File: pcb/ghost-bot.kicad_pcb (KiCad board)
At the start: 2 copper layers, 111 x 60 mm, 35 parts, among them J1 Conn_01x03_Pin, J2 Conn_01x03_Pin, J3 Conn_01x04_Pin, J4 Conn_01x02_Pin, SW1 SW_Push, SW2 SW_Push, SW3 SW_SPDT

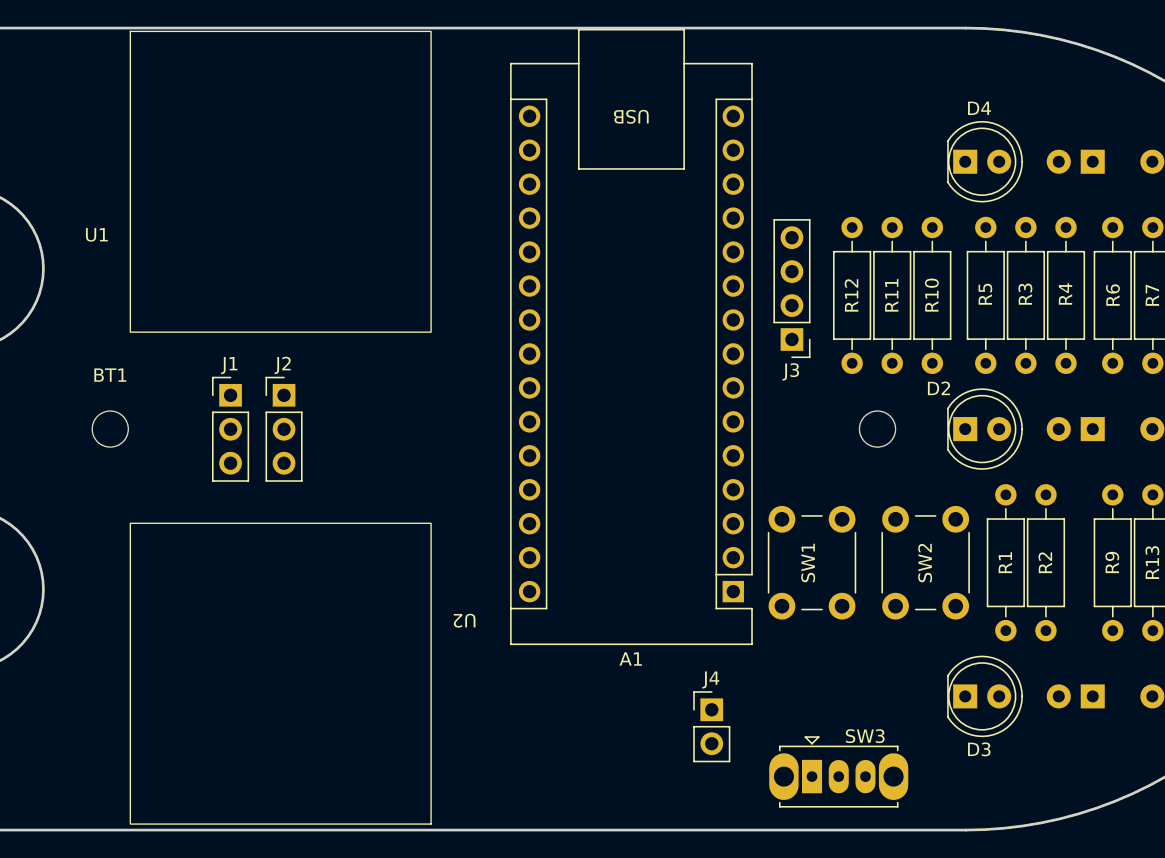
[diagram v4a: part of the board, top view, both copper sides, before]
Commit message: Minor placement changes, add strain relief for battery wires
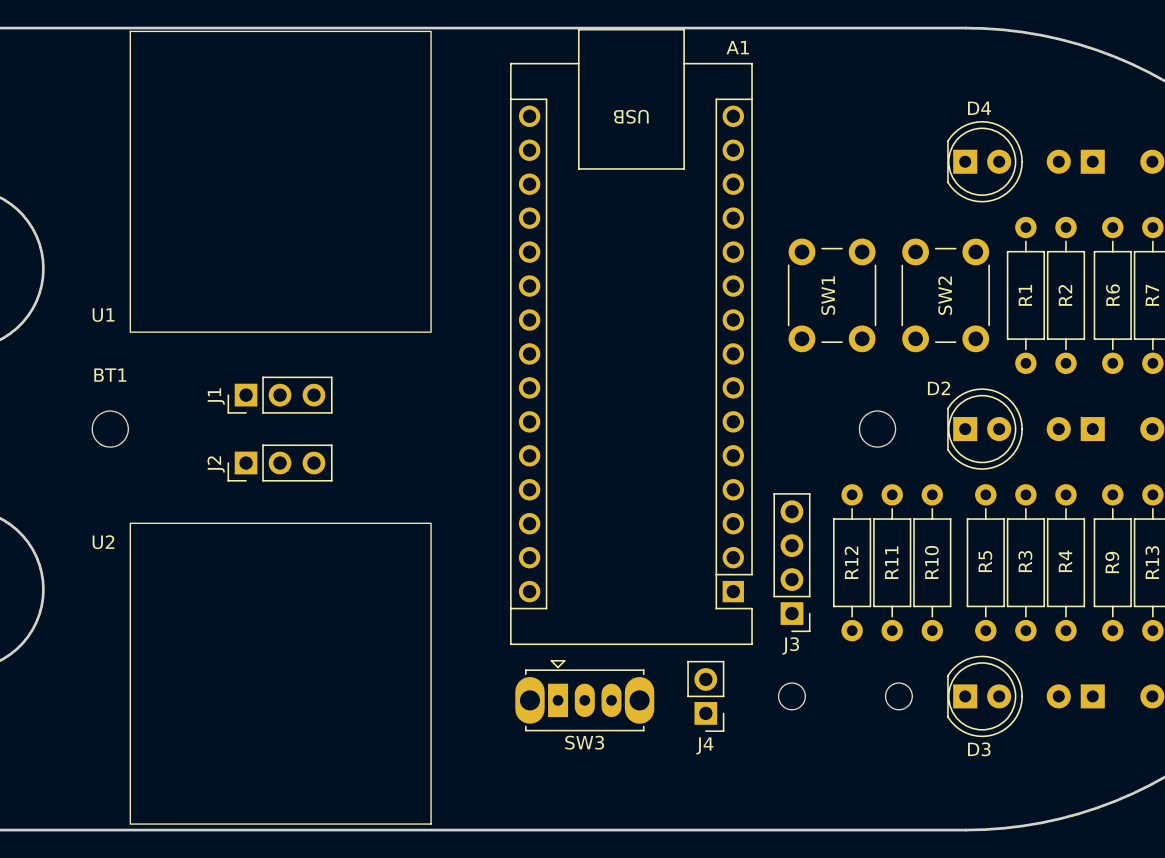
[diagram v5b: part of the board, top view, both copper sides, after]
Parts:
- added REF**: MountingHole_2.1mm, MountingHole:MountingHole_2.1mm, F.Cu at (169.5, 134.0)
- added REF**: MountingHole_2.1mm, MountingHole:MountingHole_2.1mm, F.Cu at (177.5, 134.0)
- moved J3 20.5 mm to (169.5, 127.8)
- moved R1 20.1 mm to (187.0, 109.1)
- moved R2 20.1 mm to (190.0, 109.1)
- moved SW1 20.1 mm to (170.3, 107.2)
- moved SW2 20.1 mm to (183.3, 100.8)
- moved R10 20.0 mm to (180.0, 129.1)
- moved R11 20.0 mm to (177.0, 129.1)
- moved R12 20.0 mm to (174.0, 129.1)
- moved R3 20.0 mm to (187.0, 129.1)
- moved R4 20.0 mm to (190.0, 129.1)
- moved R5 20.0 mm to (184.0, 129.1)
- moved SW3 19.8 mm to (152.0, 134.3)
- moved J2 5.81 mm to (128.7, 116.5), turned to 90 degrees
- moved J1 1.16 mm to (128.7, 111.5), turned to 90 degrees
- moved J4 0.52 mm to (163.1, 135.3), turned to 180 degrees

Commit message: WIP commit before changing layout
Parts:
- moved J1 5.08 mm to (128.7, 116.5)
- moved J2 5.08 mm to (128.7, 111.5)
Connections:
- A1 pad 21: /PD2 -> unconnected-(A1-A2-Pad21)
- A1 pad 26: unconnected-(A1-A7-Pad26) -> /PD2
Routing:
- net /PD2: track 0.00 -> 53.2 mm
- net /LED2: track 0.00 -> 52.5 mm
- net /PUSH_BTN1: track 0.00 -> 37.8 mm
- net /PUSH_BTN0: track 0.00 -> 30.7 mm
- net /LED0: track 0.00 -> 22.5 mm
- net /LED1: track 0.00 -> 20.6 mm

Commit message: Add initial routing
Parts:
- moved J3 44.5 mm to (128.7, 110.2), turned to 90 degrees
- moved REF** 27.5 mm to (150.0, 133.8), turned to 0 degrees
- moved R12 25.3 mm to (189.5, 109.1)
- moved R5 21.7 mm to (192.5, 109.1)
- moved R10 21.5 mm to (199.0, 118.9), turned to -90 degrees
- moved R9 21.2 mm to (186.5, 109.1)
- moved SW1 21.0 mm to (179.3, 126.2), turned to 180 degrees
- moved R4 15.7 mm to (202.0, 118.9), turned to -90 degrees
- moved R11 12.5 mm to (189.5, 129.1)
- moved R2 12.3 mm to (183.0, 98.9), turned to -90 degrees
- moved D2 12.3 mm to (194.7, 114.0)
- moved D3 12.3 mm to (194.7, 134.0)
- moved D4 12.3 mm to (194.7, 94.0)
- moved REF** 11.5 mm to (158.0, 133.8), turned to 0 degrees
- moved R14 10.7 mm to (196.0, 118.9), turned to -90 degrees
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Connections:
- A1 pad 12: /RGB_R -> /RGB_B
- A1 pad 14: /RGB_B -> /RGB_R
- A1 pad 20: /PD1 -> unconnected-(A1-A1-Pad20)
- A1 pad 25: unconnected-(A1-A6-Pad25) -> /PD1
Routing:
- net /PD1: track 0.00 -> 49.6 mm
- net /TRIG: track 0.00 -> 48.1 mm
- net /RGB_R: track 0.00 -> 45.8 mm
- net /RGB_G: track 0.00 -> 44.8 mm
- net /RGB_B: track 0.00 -> 43.6 mm
- net /PD0: track 0.00 -> 41.6 mm
- net /SERVO0: track 0.00 -> 40.9 mm
- net /SERVO1: track 0.00 -> 38.8 mm
- net /ECHO: track 0.00 -> 28.7 mm
- net +BATT_SW: track 0.00 -> 16.5 mm
- net /LED0: track 22.5 -> 36.5 mm
- net /PUSH_BTN1: track 37.8 -> 23.7 mm
- net /LED1: track 20.6 -> 34.5 mm
- net Net-(D6-A): track 0.00 -> 12.8 mm
- net +BATT: track 0.00 -> 11.8 mm
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- added copper zone on F.Cu, net +5V
- added copper zone on B.Cu, net GND

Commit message: Fix unconnected net
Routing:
- net +5V: track 0.00 -> 8.45 mm
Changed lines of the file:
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@@
 		(tags "Through hole pin header THT 1x02 2.54mm single row")
 		(property "Reference" "J4"
-			(at 0 -2.33 360)
+			(at 2.54 1.275 360)
 			(layer "F.SilkS")
 			(effects
@@
 	)
 	(segment
+		(start 184.275003 130.355)
+		(end 184.275003 134)
+		(width 1.5)
+		(layer "B.Cu")
+		(net 18)
+	)
+	(segment
+		(start 189.500003 109.08)
+		(end 192.500003 109.08)
+		(width 1.5)
+		(layer "B.Cu")
+		(net 18)
+	)
+	(segment
+		(start 183.000003 129.08)
+		(end 184.275003 130.355)
+		(width 1.5)
+		(layer "B.Cu")
+		(net 18)
+	)
+	(segment
